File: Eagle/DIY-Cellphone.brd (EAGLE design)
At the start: 130.8 x 58.4 mm, 67 parts, among them IC1 MEGA1284, J1 ISP, U1 MCP73831, U7 M10_HDWITHOUT_EXCLUSION, X1 BU-SMA-V, X3 CCM03-3002 R102

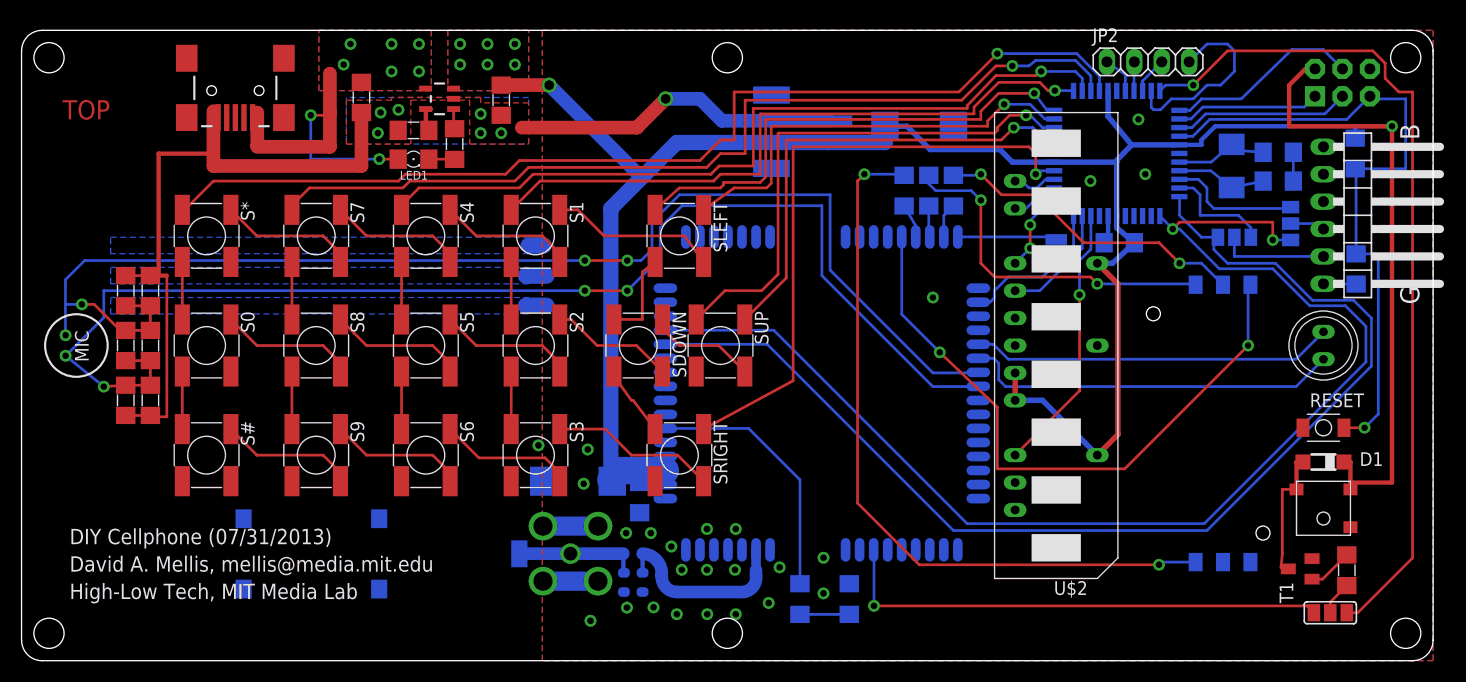
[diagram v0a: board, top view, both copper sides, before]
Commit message: Create UC15 footprint; replace M10 w/ UC15.
Warning: this board won’t work! Note that many of the traces on the
board now overlap the new pads on the UC15 (that aren’t on the M10).
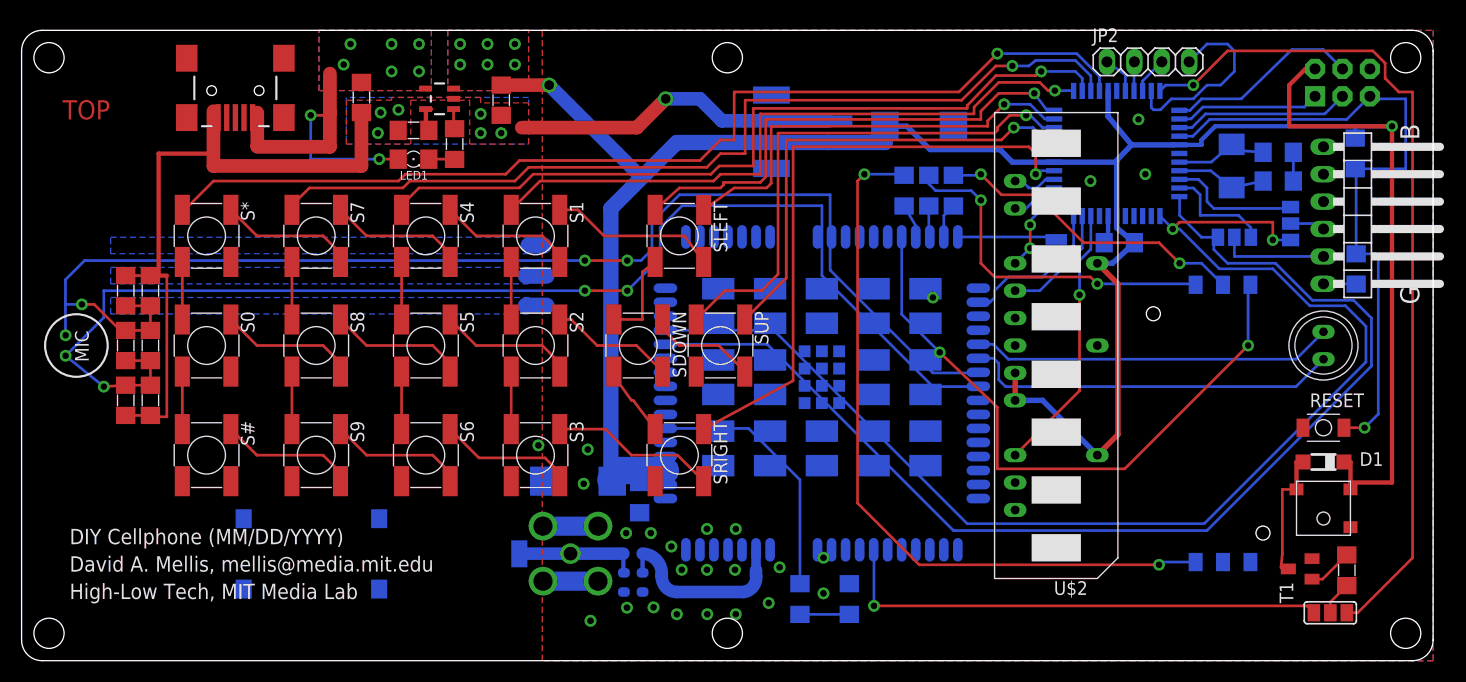
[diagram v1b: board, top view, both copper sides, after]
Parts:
- removed U7: M10_HDWITHOUT_EXCLUSION, GSM:M10_HD_WITHOUT_EXCLUSION
- added U$6: UC15, cellphone:UC15
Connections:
- net ADC0: now also U$6.P$41; no longer U7.P$41
- net ANT: now also U$6.P$43; no longer U7.P$43
- net BUZZ_M10: now also U$6.P$39; no longer U7.P$39
- net DBG_RXD: now also U$6.P$9; no longer U7.P$9
- net DBG_TXD: now also U$6.P$10; no longer U7.P$10
- net DISP_CLK: now also U$6.P$2; no longer U7.P$2
- net DISP_CS: now also U$6.P$3; no longer U7.P$3
- net DISP_D/C: now also U$6.P$4; no longer U7.P$4
- net DISP_DATA: now also U$6.P$1; no longer U7.P$1
- net DISP_RST: now also U$6.P$5; no longer U7.P$5
- net DTR: now also U$6.P$59; no longer U7.P$59
- net GND: now also U$6.P$19, U$6.P$42, U$6.P$44, U$6.P$45, U$6.P$46, U$6.P$47, U$6.P$48, U$6.P$49, U$6.P$8; no longer U7.P$19, U7.P$42, U7.P$44, U7.P$45, U7.P$46, U7.P$47, U7.P$48, U7.P$49, U7.P$8
- net GPIO0: now also U$6.P$64; no longer U7.P$64
- net KBC0: now also U$6.P$33; no longer U7.P$33
- net KBC1: now also U$6.P$34; no longer U7.P$34
- net KBC2: now also U$6.P$35; no longer U7.P$35
- net KBC3: now also U$6.P$36; no longer U7.P$36
- net KBC4: now also U$6.P$37; no longer U7.P$37
- net KBC5: now also U$6.P$38; no longer U7.P$38
- net KBR0: now also U$6.P$28; no longer U7.P$28
- net KBR1: now also U$6.P$29; no longer U7.P$29
- net KBR2: now also U$6.P$30; no longer U7.P$30
- net KBR3: now also U$6.P$31; no longer U7.P$31
- net KBR4: now also U$6.P$32; no longer U7.P$32
- net LIGHT_MOS: now also U$6.P$27; no longer U7.P$27
- net MIC1N: now also U$6.P$24; no longer U7.P$24
- net MIC1P: now also U$6.P$23; no longer U7.P$23
- net MIC2N: now also U$6.P$26; no longer U7.P$26
- net MIC2P: now also U$6.P$25; no longer U7.P$25
- net N$1: now also U$6.P$57; no longer U7.P$57
- net N$43: now also U$6.P$58; no longer U7.P$58
- net NETLIGHT: now also U$6.P$6; no longer U7.P$6
- net PWRKEY: now also U$6.P$18; no longer U7.P$18
- net RI: now also U$6.P$55; no longer U7.P$55
- net RXD1: now also U$6.P$60; no longer U7.P$60
- net SIM_CLK: now also U$6.P$14; no longer U7.P$14
- net SIM_DATA: now also U$6.P$13; no longer U7.P$13
- net SIM_RST: now also U$6.P$15; no longer U7.P$15
- net SIM_VDD: now also U$6.P$12; no longer U7.P$12
- net SPK1N: now also U$6.P$21; no longer U7.P$21
- net SPK1P: now also U$6.P$22; no longer U7.P$22
- net SPK2P: now also U$6.P$20; no longer U7.P$20
- net STATUS: now also U$6.P$54; no longer U7.P$54
- net TXD1: now also U$6.P$61; no longer U7.P$61
- net VCC: now also U$6.P$50, U$6.P$51, U$6.P$52; no longer U7.P$50, U7.P$51, U7.P$52
- net VRTC: now also U$6.P$16; no longer U7.P$16
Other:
- board text added: "DIY Cellphone (MM/DD/YYYY)"
- board text removed: "DIY Cellphone (07/31/2013)"

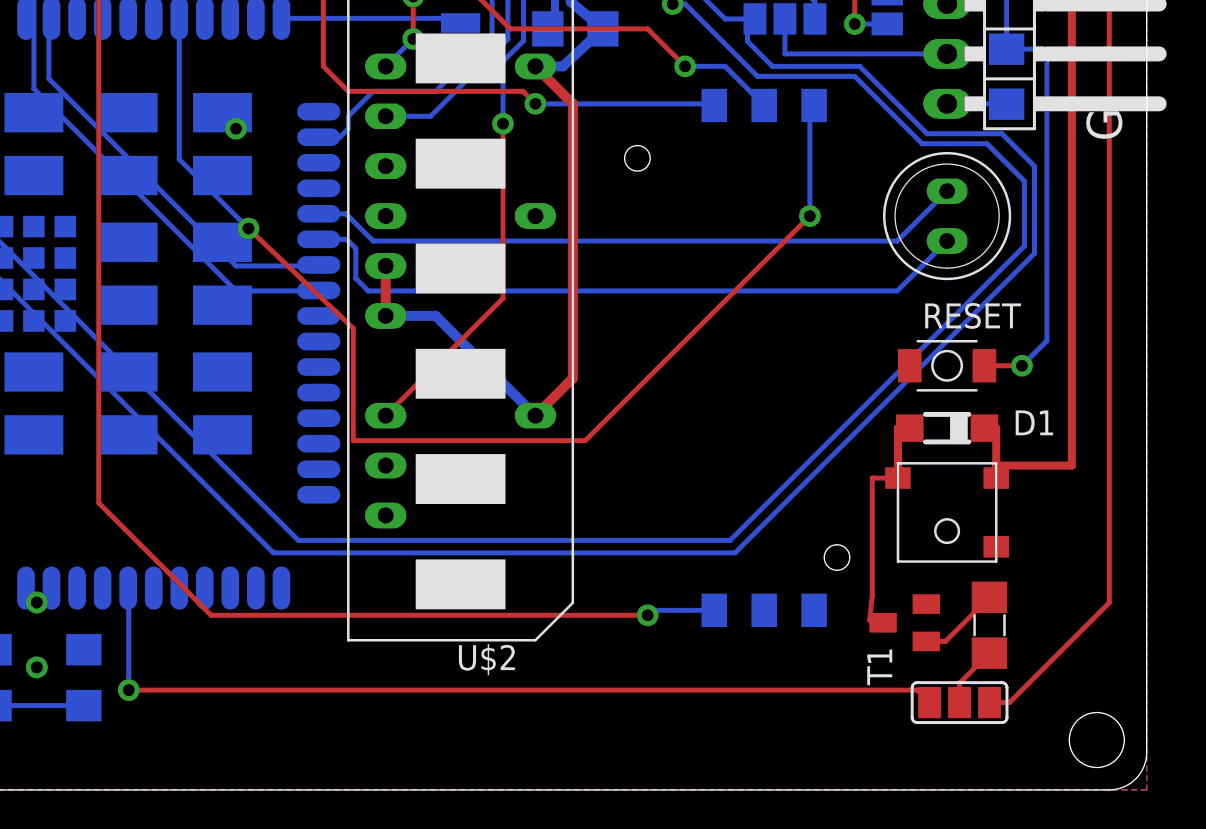
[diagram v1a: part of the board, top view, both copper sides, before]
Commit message: Connect buzzer directly to microcontroller.
Remove solder jumper that allows it to go to the Quectel module, since
the UC15 drops the buzzer pin.
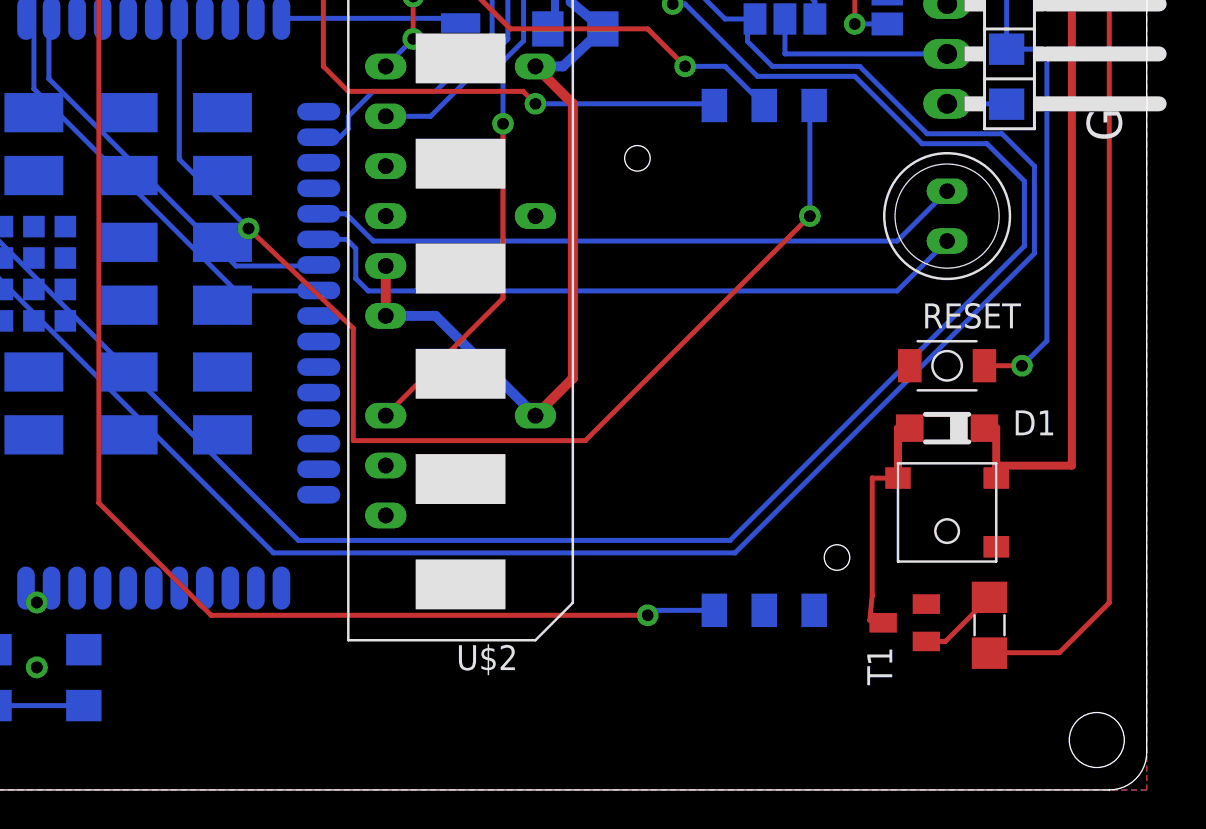
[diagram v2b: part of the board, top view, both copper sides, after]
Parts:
- removed SJ3: (no value), jumper:SJ_2
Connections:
- removed net BUZZ: R6.1, SJ3.2
- net BUZZ_AVR: now also R6.1; no longer SJ3.1
- net BUZZ_M10: no longer SJ3.3
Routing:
- net BUZZ_M10: track 46.3 -> 0.00 mm, vias 1 -> 0
- net BUZZ: track 3.15 -> 0.00 mm
- net BUZZ_AVR: track 78.7 -> 77.7 mm
- net GND: vias 32 -> 31
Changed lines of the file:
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@@
 </element>
 <element name="U$2" library="cellphone" package="HCMS-[23]97X" value="HCMS-[23]97X" x="95.885" y="29.21" rot="R90"/>
-<element name="SJ3" library="jumper" package="SJ_2" value="" x="121.285" y="4.445" smashed="yes" rot="R180">
-<attribute name="VALUE" x="121.3851" y="4.445" size="0.02" layer="27" rot="R180"/>
-</element>
 <element name="JP2" library="pinhead" package="1X04" value="" x="104.394" y="55.499"/>
 <element name="U$6" library="cellphone" package="UC15" value="UC15" x="88.665" y="39.274" rot="MR270"/>
@@
 <wire x1="46.736" y1="32.893" x2="48.641" y2="32.893" width="1.524" layer="16"/>
 <via x="104.14" y="45.085" extent="1-16" drill="0.6"/>
-<via x="84.455" y="33.655" extent="1-16" drill="0.6"/>
 <contactref element="RESET" pad="P$1"/>
 <polygon width="0.254" layer="1" thermals="no">
@@
 <contactref element="U$6" pad="P$19"/>
 <contactref element="U$6" pad="P$8"/>
-<wire x1="76.365" y1="39.274" x2="84.455" y2="33.655" width="0" layer="19" extent="16-16"/>
+<wire x1="120.65" y1="47.625" x2="124.949" y2="54.848" width="0" layer="19" extent="1-1"/>
+<wire x1="117.859" y1="47.117" x2="120.65" y2="47.625" width="0" layer="19" extent="16-16"/>
+<wire x1="107.292" y1="47.006" x2="117.859" y2="47.117" width="0" layer="19" extent="16-16"/>
+<wire x1="104.14" y1="45.085" x2="107.292" y2="47.006" width="0" layer="19" extent="16-16"/>
+<wire x1="103.505" y1="50.165" x2="107.292" y2="47.006" width="0" layer="19" extent="16-16"/>
+<wire x1="101.492" y1="52.806" x2="103.505" y2="50.165" width="0" layer="19" extent="16-16"/>
+<wire x1="99.06" y1="44.45" x2="104.14" y2="45.085" width="0" layer="19" extent="1-1"/>
+<wire x1="100.692" y1="41.206" x2="99.06" y2="44.45" width="0" layer="19" extent="16-16"/>
+<wire x1="95.692" y1="47.006" x2="99.06" y2="44.45" width="0" layer="19" extent="16-16"/>
+<wire x1="95.885" y1="32.337" x2="100.327" y2="38.735" width="0" layer="19" extent="16-16"/>
+<wire x1="92.075" y1="31.75" x2="95.885" y2="32.337" width="0" layer="19" extent="16-16"/>
+<wire x1="92.075" y1="29.21" x2="92.075" y2="31.75" width="0" layer="19" extent="1-1"/>
+<wire x1="88.839" y1="31.75" x2="92.075" y2="31.75" width="0" layer="19" extent="16-16"/>
+<wire x1="99.695" y1="29.21" x2="95.885" y2="32.337" width="0" layer="19" extent="16-16"/>
+<wire x1="86.36" y1="49.53" x2="95.692" y2="47.006" width="0" layer="19" extent="16-16"/>
+<wire x1="74.803" y1="50.038" x2="86.36" y2="49.53" width="0" layer="19" extent="16-16"/>
+<wire x1="74.693" y1="50.022" x2="74.803" y2="50.038" width="0" layer="19" extent="16-16"/>
+<wire x1="44.45" y1="48.895" x2="46.355" y2="49.403" width="0" layer="19" extent="1-1"/>
+<wire x1="44.45" y1="50.543" x2="44.45" y2="48.895" width="0" layer="19" extent="1-1"/>
+<wire x1="42.545" y1="48.895" x2="44.45" y2="48.895" width="0" layer="19" extent="1-1"/>
+<wire x1="42.545" y1="50.673" x2="42.545" y2="48.895" width="0" layer="19" extent="1-1"/>
+<wire x1="40.0351" y1="52.07" x2="42.545" y2="50.673" width="0" layer="19" extent="1-1"/>
+<wire x1="34.925" y1="51.054" x2="40.0351" y2="52.07" width="0" layer="19" extent="1-1"/>
+<wire x1="33.274" y1="50.8" x2="34.925" y2="51.054" width="0" layer="19" extent="1-1"/>
+<wire x1="31.496" y1="50.797" x2="33.274" y2="50.8" width="0" layer="19" extent="1-1"/>
+<wire x1="34.9" y1="49.149" x2="34.925" y2="51.054" width="0" layer="19" extent="1-1"/>
+<wire x1="33.02" y1="48.895" x2="34.9" y2="49.149" width="0" layer="19" extent="1-1"/>
+<wire x1="46.99" y1="38.481" x2="44.45" y2="48.895" width="0" layer="19" extent="16-16"/>
+<wire x1="46.736" y1="35.687" x2="46.99" y2="38.481" width="0" layer="19" extent="16-16"/>
+<wire x1="46.736" y1="32.893" x2="46.736" y2="35.687" width="0" layer="19" extent="16-16"/>
+<wire x1="76.365" y1="39.274" x2="74.803" y2="50.038" width="0" layer="19" extent="16-16"/>
+<wire x1="47.898" y1="19.955" x2="48.641" y2="32.893" width="0" layer="19" extent="16-16"/>
+<wire x1="48.387" y1="16.637" x2="47.898" y2="19.955" width="0" layer="19" extent="16-16"/>
+<wire x1="52.089" y1="16.399" x2="48.387" y2="16.637" width="0" layer="19" extent="16-16"/>
+<wire x1="52.47" y1="19.574" x2="52.089" y2="16.399" width="0" layer="19" extent="1-1"/>
+<wire x1="53.4197" y1="12.4719" x2="52.089" y2="16.399" width="0" layer="19" extent="1-1"/>
+<wire x1="56.026" y1="11.827" x2="53.4197" y2="12.4719" width="0" layer="19" extent="1-1"/>
+<wire x1="57.277" y1="13.713" x2="56.026" y2="11.827" width="0" layer="19" extent="16-16"/>
+<wire x1="58.312" y1="11.827" x2="57.277" y2="13.713" width="0" layer="19" extent="16-16"/>
+<wire x1="60.217" y1="10.5824" x2="58.312" y2="11.827" width="0" layer="19" extent="1-1"/>
+<wire x1="61.565" y1="10.274" x2="60.217" y2="10.5824" width="0" layer="19" extent="16-16"/>
+<wire x1="62.865" y1="10.274" x2="61.565" y2="10.274" width="0" layer="19" extent="16-16"/>
+<wire x1="64.165" y1="10.274" x2="62.865" y2="10.274" width="0" layer="19" extent="16-16"/>
+<wire x1="65.465" y1="10.274" x2="64.165" y2="10.274" width="0" layer="19" extent="16-16"/>
+<wire x1="66.765" y1="10.274" x2="65.465" y2="10.274" width="0" layer="19" extent="16-16"/>
+<wire x1="61.1822" y1="8.4234" x2="61.565" y2="10.274" width="0" layer="19" extent="16-16"/>
+<wire x1="66.1098" y1="8.4234" x2="65.465" y2="10.274" width="0" layer="19" extent="16-16"/>
+<wire x1="63.519" y1="8.4234" x2="62.865" y2="10.274" width="0" layer="19" extent="16-16"/>
+<wire x1="66.186" y1="12.208" x2="66.765" y2="10.274" width="0" layer="19" extent="16-16"/>
+<wire x1="63.519" y1="12.208" x2="62.865" y2="10.274" width="0" layer="19" extent="16-16"/>
+<wire x1="69.365" y1="10.274" x2="66.765" y2="10.274" width="0" layer="19" extent="16-16"/>
+<wire x1="70.25" y1="8.652" x2="69.365" y2="10.274" width="0" layer="19" extent="16-16"/>
+<wire x1="59.665" y1="15.024" x2="57.277" y2="13.713" width="0" layer="19" extent="16-16"/>
+<wire x1="69.234" y1="5.35" x2="70.25" y2="8.652" width="0" layer="19" extent="1-1"/>
+<wire x1="66.186" y1="4.3086" x2="69.234" y2="5.35" width="0" layer="19" extent="1-1"/>
+<wire x1="63.5444" y1="4.3086" x2="66.186" y2="4.3086" width="0" layer="19" extent="1-1"/>
+<wire x1="60.725" y1="4.3086" x2="63.5444" y2="4.3086" width="0" layer="19" extent="1-1"/>
+<wire x1="58.566" y1="4.9436" x2="60.725" y2="4.3086" width="0" layer="19" extent="1-1"/>
+<wire x1="57.55" y1="6.366" x2="58.566" y2="4.9436" width="0" layer="19" extent="16-16"/>
+<wire x1="55.8228" y1="6.366" x2="57.55" y2="6.366" width="0" layer="19" extent="16-16"/>
+<wire x1="56.1022" y1="4.9182" x2="55.8228" y2="6.366" width="0" layer="19" extent="16-16"/>
+<wire x1="53.4197" y1="7.3721" x2="55.8228" y2="6.366" width="0" layer="19" extent="16-16"/>
+<wire x1="52.724" y1="3.699" x2="56.1022" y2="4.9182" width="0" layer="19" extent="1-1"/>
+<wire x1="74.314" y1="9.541" x2="70.25" y2="8.652" width="0" layer="19" extent="1-1"/>
+<wire x1="74.314" y1="6.239" x2="74.314" y2="9.541" width="0" layer="19" extent="1-1"/>
+<wire x1="76.708" y1="7.137" x2="74.314" y2="6.239" width="0" layer="19" extent="16-16"/>
+<wire x1="118.75" y1="21.59" x2="99.695" y2="29.21" width="0" layer="19" extent="1-1"/>
+<wire x1="119.591" y1="9.459" x2="118.75" y2="21.59" width="0" layer="19" extent="1-1"/>
+<wire x1="113.881" y1="9.14" x2="119.591" y2="9.459" width="0" layer="19" extent="1-16"/>
 </signal>
 <signal name="DISP_DATA">
@@
 <signal name="ADC0">
 <contactref element="U$6" pad="P$41"/>
-</signal>
-<signal name="BUZZ">
-<contactref element="R6" pad="1"/>
-<contactref element="SJ3" pad="2"/>
-<wire x1="121.285" y1="4.445" x2="121.285" y2="5.436" width="0.254" layer="1"/>
-<wire x1="121.285" y1="5.436" x2="122.809" y2="6.96" width="0.254" layer="1"/>
 </signal>
 <signal name="KBC5">
@@
 <signal name="BUZZ_AVR">
 <contactref element="IC1" pad="44"/>
-<contactref element="SJ3" pad="1"/>
 <wire x1="128.905" y1="9.525" x2="128.905" y2="52.705" width="0.254" layer="1"/>
 <wire x1="125.222" y1="56.515" x2="111.76" y2="56.515" width="0.254" layer="1"/>
@@
 <wire x1="106.026" y1="53.34" x2="105.492" y2="52.806" width="0.254" layer="16"/>
 <wire x1="125.222" y1="56.515" x2="126.365" y2="55.372" width="0.254" layer="1"/>
-<wire x1="122.809" y1="4.445" x2="123.825" y2="4.445" width="0.254" layer="1"/>
-<wire x1="123.825" y1="4.445" x2="128.905" y2="9.525" width="0.254" layer="1"/>
+<wire x1="126.365" y1="6.985" x2="128.905" y2="9.525" width="0.254" layer="1"/>
 <wire x1="128.905" y1="52.705" x2="127.635" y2="52.705" width="0.254" layer="1"/>
 <wire x1="127.635" y1="52.705" x2="126.365" y2="53.975" width="0.254" layer="1"/>
 <wire x1="126.365" y1="53.975" x2="126.365" y2="55.372" width="0.254" layer="1"/>
+<contactref element="R6" pad="1"/>
+<wire x1="126.365" y1="6.985" x2="122.809" y2="6.985" width="0.254" layer="1"/>
+<wire x1="122.809" y1="6.985" x2="122.809" y2="6.96" width="0.254" layer="1"/>
 </signal>
 <signal name="N$43">
@@
 </signal>
 <signal name="BUZZ_M10">
-<contactref element="SJ3" pad="3"/>
-<wire x1="78.965" y1="10.274" x2="78.994" y2="10.274" width="0.254" layer="16"/>
-<wire x1="78.994" y1="10.274" x2="78.994" y2="5.08" width="0.254" layer="16"/>
-<via x="78.994" y="5.08" extent="1-16" drill="0.6"/>
-<wire x1="78.994" y1="5.08" x2="119.126" y2="5.08" width="0.254" layer="1"/>
-<wire x1="119.126" y1="5.08" x2="119.761" y2="4.445" width="0.254" layer="1"/>
 <contactref element="U$6" pad="P$39"/>
 </signal>
